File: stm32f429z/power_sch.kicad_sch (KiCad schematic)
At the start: 14 parts

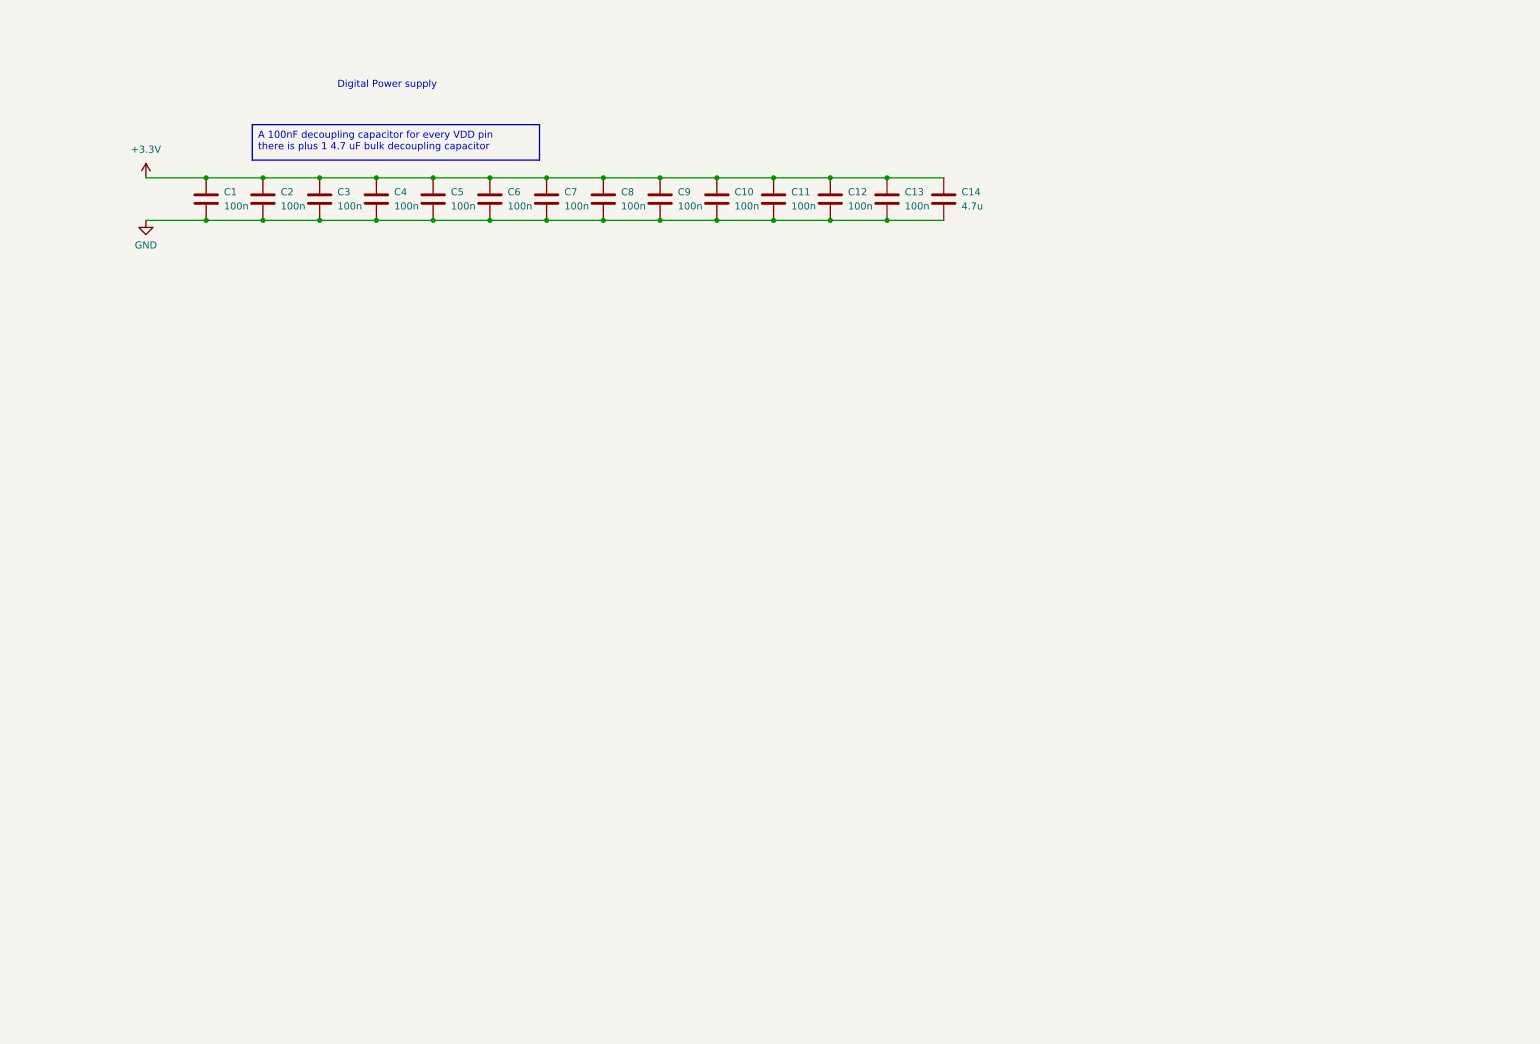
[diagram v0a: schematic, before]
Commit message: finished schematics and mostly finished the routing for the pcb
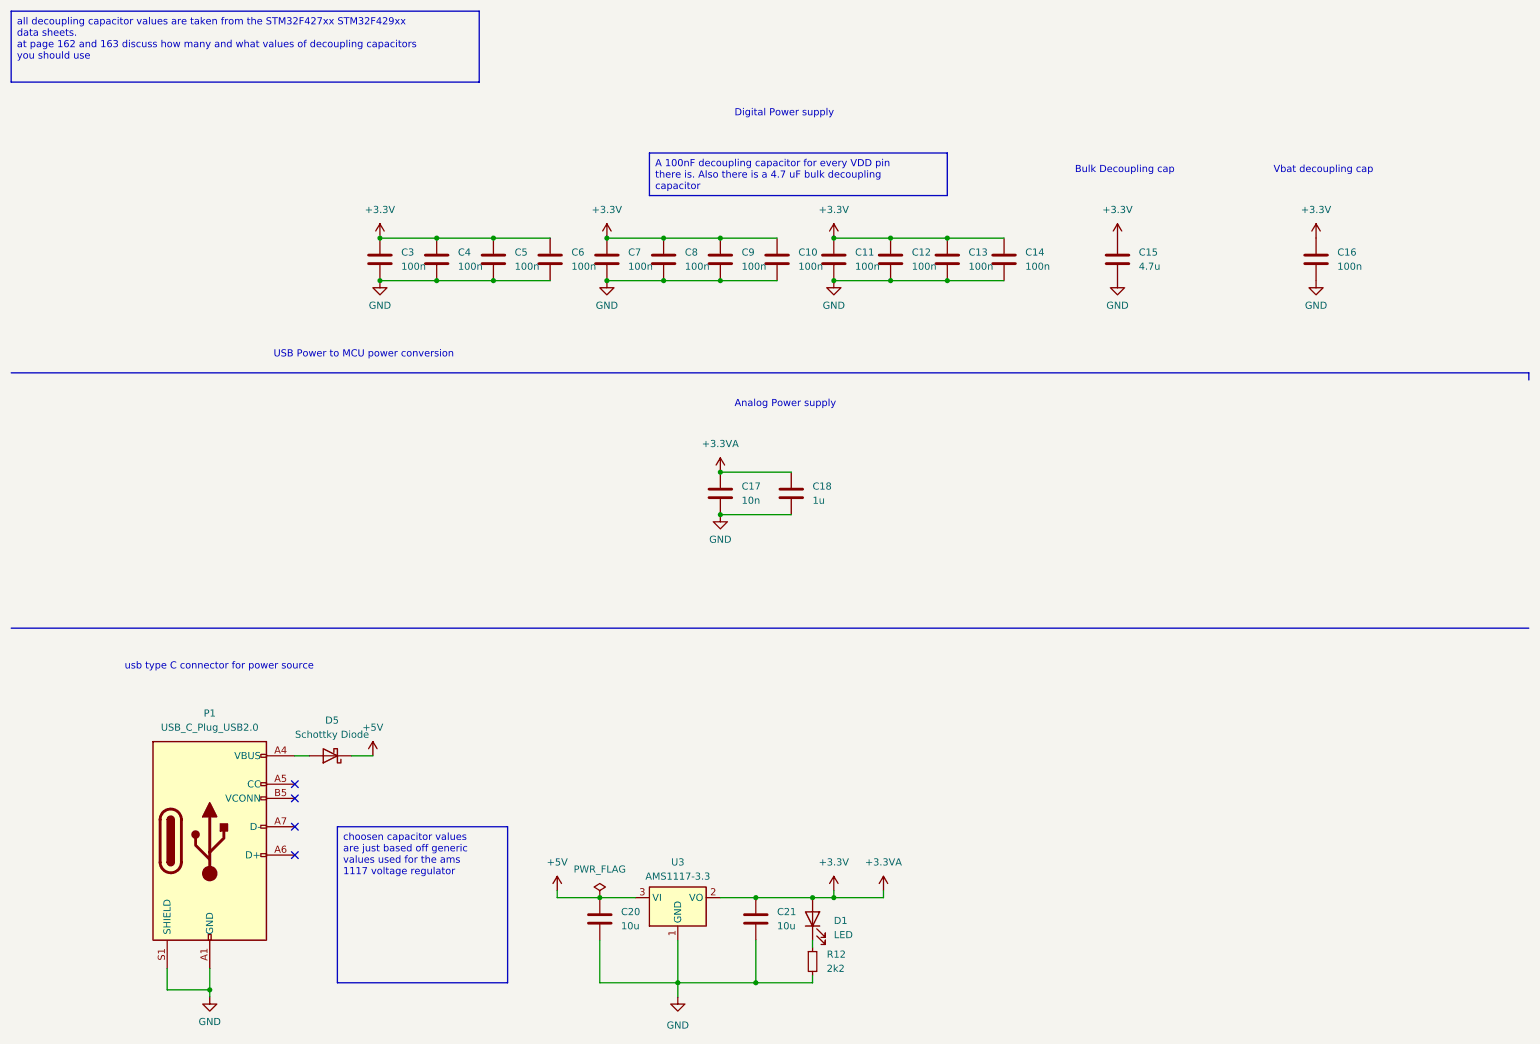
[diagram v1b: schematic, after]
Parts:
- removed C13: 100n, symbol Device:C
- added C16: 100n, Capacitor_SMD:C_0603_1608Metric_Pad1.08x0.95mm_HandSolder, symbol Device:C
- added C17: 10n, Capacitor_SMD:C_0603_1608Metric_Pad1.08x0.95mm_HandSolder, symbol Device:C
- added C18: 1u, Capacitor_SMD:C_0603_1608Metric_Pad1.08x0.95mm_HandSolder, symbol Device:C
- added C20, C21: 10u, Capacitor_SMD:C_0603_1608Metric_Pad1.08x0.95mm_HandSolder, symbol Device:C
- added D1: LED, LED_SMD:LED_0603_1608Metric_Pad1.05x0.95mm_HandSolder, symbol Device:LED
- added D5: Schottky Diode, Diode_SMD:D_0603_1608Metric_Pad1.05x0.95mm_HandSolder, symbol Device:D_Schottky
- added P1: USB_C_Plug_USB2.0, Connector_USB:USB_C_Receptacle_G-Switch_GT-USB-7010ASV, symbol Connector:USB_C_Plug_USB2.0
- added R12: 2k2, Resistor_SMD:R_0603_1608Metric_Pad0.98x0.95mm_HandSolder, symbol Device:R_Small
- added U3: AMS1117-3.3, Package_TO_SOT_SMD:SOT-223-3_TabPin2, symbol Regulator_Linear:AMS1117-3.3
- C10: renamed from C8; footprint (none) -> Capacitor_SMD:C_0603_1608Metric_Pad1.08x0.95mm_HandSolder
- C11: renamed from C9; footprint (none) -> Capacitor_SMD:C_0603_1608Metric_Pad1.08x0.95mm_HandSolder
- C12: renamed from C10; footprint (none) -> Capacitor_SMD:C_0603_1608Metric_Pad1.08x0.95mm_HandSolder
- C13: renamed from C11; footprint (none) -> Capacitor_SMD:C_0603_1608Metric_Pad1.08x0.95mm_HandSolder
- C14: renamed from C12; footprint (none) -> Capacitor_SMD:C_0603_1608Metric_Pad1.08x0.95mm_HandSolder
- C15: renamed from C14; footprint (none) -> Capacitor_SMD:C_0603_1608Metric_Pad1.08x0.95mm_HandSolder
- C3: renamed from C1; footprint (none) -> Capacitor_SMD:C_0603_1608Metric_Pad1.08x0.95mm_HandSolder
- C4: renamed from C2; footprint (none) -> Capacitor_SMD:C_0603_1608Metric_Pad1.08x0.95mm_HandSolder
- C5: renamed from C3; footprint (none) -> Capacitor_SMD:C_0603_1608Metric_Pad1.08x0.95mm_HandSolder
- C6: renamed from C4; footprint (none) -> Capacitor_SMD:C_0603_1608Metric_Pad1.08x0.95mm_HandSolder
- C7: renamed from C5; footprint (none) -> Capacitor_SMD:C_0603_1608Metric_Pad1.08x0.95mm_HandSolder
- C8: renamed from C6; footprint (none) -> Capacitor_SMD:C_0603_1608Metric_Pad1.08x0.95mm_HandSolder
- C9: renamed from C7; footprint (none) -> Capacitor_SMD:C_0603_1608Metric_Pad1.08x0.95mm_HandSolder
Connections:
- net +3.3V: now also C16.1, C17.1, C18.1, C21.1, D1.2 (A), U3.2 (VO)
- net GND: now also C16.2, C17.2, C18.2, C20.2, C21.2, P1.A1 (GND), P1.A12 (GND), P1.B1 (GND), P1.B12 (GND), P1.S1 (SHIELD), R12.2, U3.1 (GND)
- new net: D1.1 (K), R12.1
- new net: D5.2 (A), P1.A4 (VBUS), P1.A9 (VBUS), P1.B4 (VBUS), P1.B9 (VBUS)
- new net +5V: C20.1, D5.1 (K), U3.3 (VI)
- no-connect marks 0 -> 4
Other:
- note added: "Analog Power supply"
- note added: "Bulk Decoupling cap"
- note added: "USB Power to MCU power conversion"
- note added: "Vbat decoupling cap"
- note added: "usb type C connector for power source"
- moved on the sheet: C10, C11, C12, C13, C14, C15, C3, C4, C5, C6, C7, C8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

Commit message: removed alot of the silk screen, changed oscillator foor print and added GPIOs
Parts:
- P1: footprint Connector_USB:USB_C_Receptacle_G-Switch_GT-USB-7010ASV -> Connector_USB:USB_C_Receptacle_GCT_USB4085
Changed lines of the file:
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@@
       (effects (font (size 1.27 1.27)))
     )
-    (property "Footprint" "Connector_USB:USB_C_Receptacle_G-Switch_GT-USB-7010ASV" (at 52.07 161.29 0)
+    (property "Footprint" "Connector_USB:USB_C_Receptacle_GCT_USB4085" (at 52.07 161.29 0)
       (effects (font (size 1.27 1.27)) hide)
     )

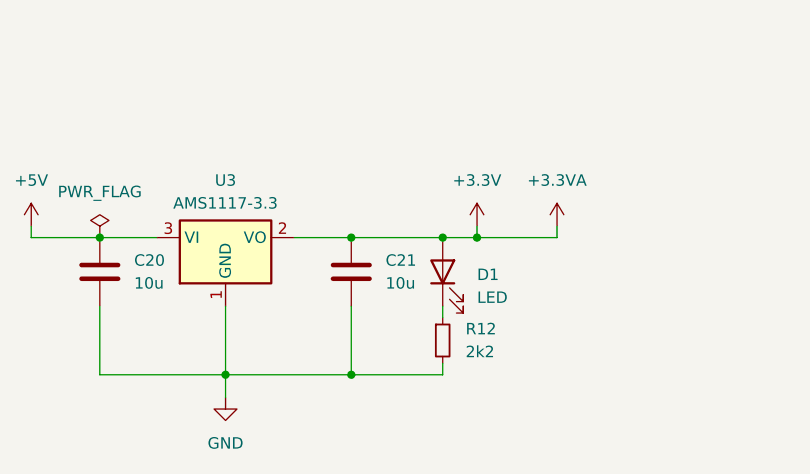
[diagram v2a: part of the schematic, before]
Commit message: changed logging schematic, tweaked some parts of the schematic
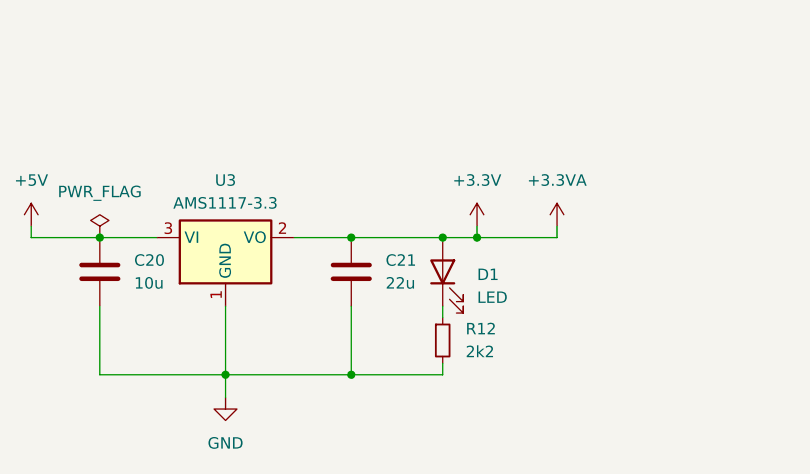
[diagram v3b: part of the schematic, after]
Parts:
- C21: value 10u -> 22u
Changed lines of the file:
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@@
       (effects (font (size 1.27 1.27)) (justify left))
     )
-    (property "Value" "10u" (at 149.86 176.53 0)
+    (property "Value" "22u" (at 149.86 176.53 0)
       (effects (font (size 1.27 1.27)) (justify left))
     )

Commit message: changed some footprints, removed dimensions( was causing issues), addd a gerber filter for manufacturing(probably should be regenerated), added a BOM list
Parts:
- D5: footprint Diode_SMD:D_0603_1608Metric_Pad1.05x0.95mm_HandSolder -> Diode_SMD:D_SMA-SMB_Universal_Handsoldering
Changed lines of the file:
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@@
       (effects (font (size 1.27 1.27)))
     )
-    (property "Footprint" "Diode_SMD:D_0603_1608Metric_Pad1.05x0.95mm_HandSolder" (at 69.85 146.05 0)
+    (property "Footprint" "Diode_SMD:D_SMA-SMB_Universal_Handsoldering" (at 69.85 146.05 0)
       (effects (font (size 1.27 1.27)) hide)
     )

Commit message: usb footprint changes, Silkscreen markers for pin 1 in ICs and polarity for other components. Edited excel BOM list and kicad list for BOM cost.
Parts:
- C10, C11, C12, C13, C14, C16, C3, C4, C5, C6, C7, C8, C9: JLCpart# (none) -> C76599
- C15: JLCpart# (none) -> C19666
- C17: JLCpart# (none) -> C57112
- C18: JLCpart# (none) -> C15849
- C20, C21: JLCpart# (none) -> C96446
- D1: JLCpart# (none) -> C72038
- D5: JLCpart# (none) -> C2480
- R12: JLCpart# (none) -> C427273
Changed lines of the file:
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@@
+      (effects (font (size 1.27 1.27)) hide)
+    )
+    (property "JLCpart#" "C427273" (at 156.21 182.88 0)
       (effects (font (size 1.27 1.27)) hide)
     )
@@
       (effects (font (size 1.27 1.27)) hide)
     )
+    (property "JLCpart#" "C76599" (at 160.02 57.15 0)
+      (effects (font (size 1.27 1.27)) hide)
+    )
     (pin "1")
     (pin "2")
@@
     )
     (property "Datasheet" "http://www.advanced-monolithic.com/pdf/ds1117.pdf" (at 134.62 177.8 0)
+      (effects (font (size 1.27 1.27)) hide)
+    )
+    (property "JLCpart#" "" (at 132.08 171.45 0)
       (effects (font (size 1.27 1.27)) hide)
     )
@@
       (effects (font (size 1.27 1.27)) hide)
     )
+    (property "JLCpart#" "C76599" (at 139.7 57.15 0)
+      (effects (font (size 1.27 1.27)) hide)
+    )
     (pin "1")
     (pin "2")
@@
       (effects (font (size 1.27 1.27)) hide)
     )
+    (property "JLCpart#" "C15849" (at 152.4 99.06 0)
+      (effects (font (size 1.27 1.27)) hide)
+    )
     (pin "1")
     (pin "2")
@@
     )
     (property "Datasheet" "~" (at 88.9 57.15 0)
+      (effects (font (size 1.27 1.27)) hide)
+    )
+    (property "JLCpart#" "C76599" (at 88.9 57.15 0)
       (effects (font (size 1.27 1.27)) hide)
     )
@@
       (effects (font (size 1.27 1.27)) hide)
     )
+    (property "JLCpart#" "C76599" (at 190.5 57.15 0)
+      (effects (font (size 1.27 1.27)) hide)
+    )
     (pin "1")
     (pin "2")
@@
     )
     (property "Datasheet" "~" (at 149.86 57.15 0)
+      (effects (font (size 1.27 1.27)) hide)
+    )
+    (property "JLCpart#" "C76599" (at 149.86 57.15 0)
       (effects (font (size 1.27 1.27)) hide)
     )
@@
       (effects (font (size 1.27 1.27)) hide)
     )
+    (property "JLCpart#" "C72038" (at 156.21 175.26 0)
+      (effects (font (size 1.27 1.27)) hide)
+    )
     (pin "1")
     (pin "2")
@@
       (effects (font (size 1.27 1.27)) hide)
     )
+    (property "JLCpart#" "C76599" (at 78.74 57.15 0)
+      (effects (font (size 1.27 1.27)) hide)
+    )
     (pin "1")
     (pin "2")
@@
       (effects (font (size 1.27 1.27)) hide)
     )
+    (property "JLCpart#" "C76599" (at 129.54 57.15 0)
+      (effects (font (size 1.27 1.27)) hide)
+    )
     (pin "1")
     (pin "2")
@@
     )
     (property "Datasheet" "https://www.usb.org/sites/default/files/documents/usb_type-c.zip" (at 52.07 161.29 0)
+      (effects (font (size 1.27 1.27)) hide)
+    )
+    (property "JLCpart#" "" (at 48.26 161.29 0)
       (effects (font (size 1.27 1.27)) hide)
     )
@@
       (effects (font (size 1.27 1.27)) hide)
     )
+    (property "JLCpart#" "C2480" (at 69.85 146.05 0)
+      (effects (font (size 1.27 1.27)) hide)
+    )
     (pin "1")
     (pin "2")
@@
     )
     (property "Datasheet" "~" (at 146.05 175.26 0)
+      (effects (font (size 1.27 1.27)) hide)
+    )
+    (property "JLCpart#" "C96446" (at 146.05 175.26 0)
       (effects (font (size 1.27 1.27)) hide)
     )
@@
       (effects (font (size 1.27 1.27)) hide)
     )
+    (property "JLCpart#" "C76599" (at 99.06 57.15 0)
+      (effects (font (size 1.27 1.27)) hide)
+    )
     (pin "1")
     (pin "2")
@@
       (effects (font (size 1.27 1.27)) hide)
     )
+    (property "JLCpart#" "C76599" (at 246.38 57.15 0)
+      (effects (font (size 1.27 1.27)) hide)
+    )
     (pin "1")
     (pin "2")
@@
       (effects (font (size 1.27 1.27)) hide)
     )
+    (property "JLCpart#" "C76599" (at 109.22 57.15 0)
+      (effects (font (size 1.27 1.27)) hide)
+    )
     (pin "1")
     (pin "2")
@@
       (effects (font (size 1.27 1.27)) hide)
     )
+    (property "JLCpart#" "C19666" (at 210.82 57.15 0)
+      (effects (font (size 1.27 1.27)) hide)
+    )
     (pin "1")
     (pin "2")
@@
     )
     (property "Datasheet" "~" (at 139.7 99.06 0)
+      (effects (font (size 1.27 1.27)) hide)
+    )
+    (property "JLCpart#" "C57112" (at 139.7 99.06 0)
       (effects (font (size 1.27 1.27)) hide)
     )
@@
       (effects (font (size 1.27 1.27)) hide)
     )
+    (property "JLCpart#" "C76599" (at 119.38 57.15 0)
+      (effects (font (size 1.27 1.27)) hide)
+    )
     (pin "1")
     (pin "2")
@@
       (effects (font (size 1.27 1.27)) hide)
     )
+    (property "JLCpart#" "C76599" (at 180.34 57.15 0)
+      (effects (font (size 1.27 1.27)) hide)
+    )
     (pin "1")
     (pin "2")
@@
     )
     (property "Datasheet" "~" (at 118.11 175.26 0)
+      (effects (font (size 1.27 1.27)) hide)
+    )
+    (property "JLCpart#" "C96446" (at 118.11 175.26 0)
       (effects (font (size 1.27 1.27)) hide)
     )
@@
       (effects (font (size 1.27 1.27)) hide)
     )
+    (property "JLCpart#" "C76599" (at 170.18 57.15 0)
+      (effects (font (size 1.27 1.27)) hide)
+    )
